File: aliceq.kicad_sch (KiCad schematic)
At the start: 174 parts, among them J1 ISP-6, SW1 SW_Push, U1 ATmega32U4-AU, U2 PRTR5V0U2X, Y1 CLK

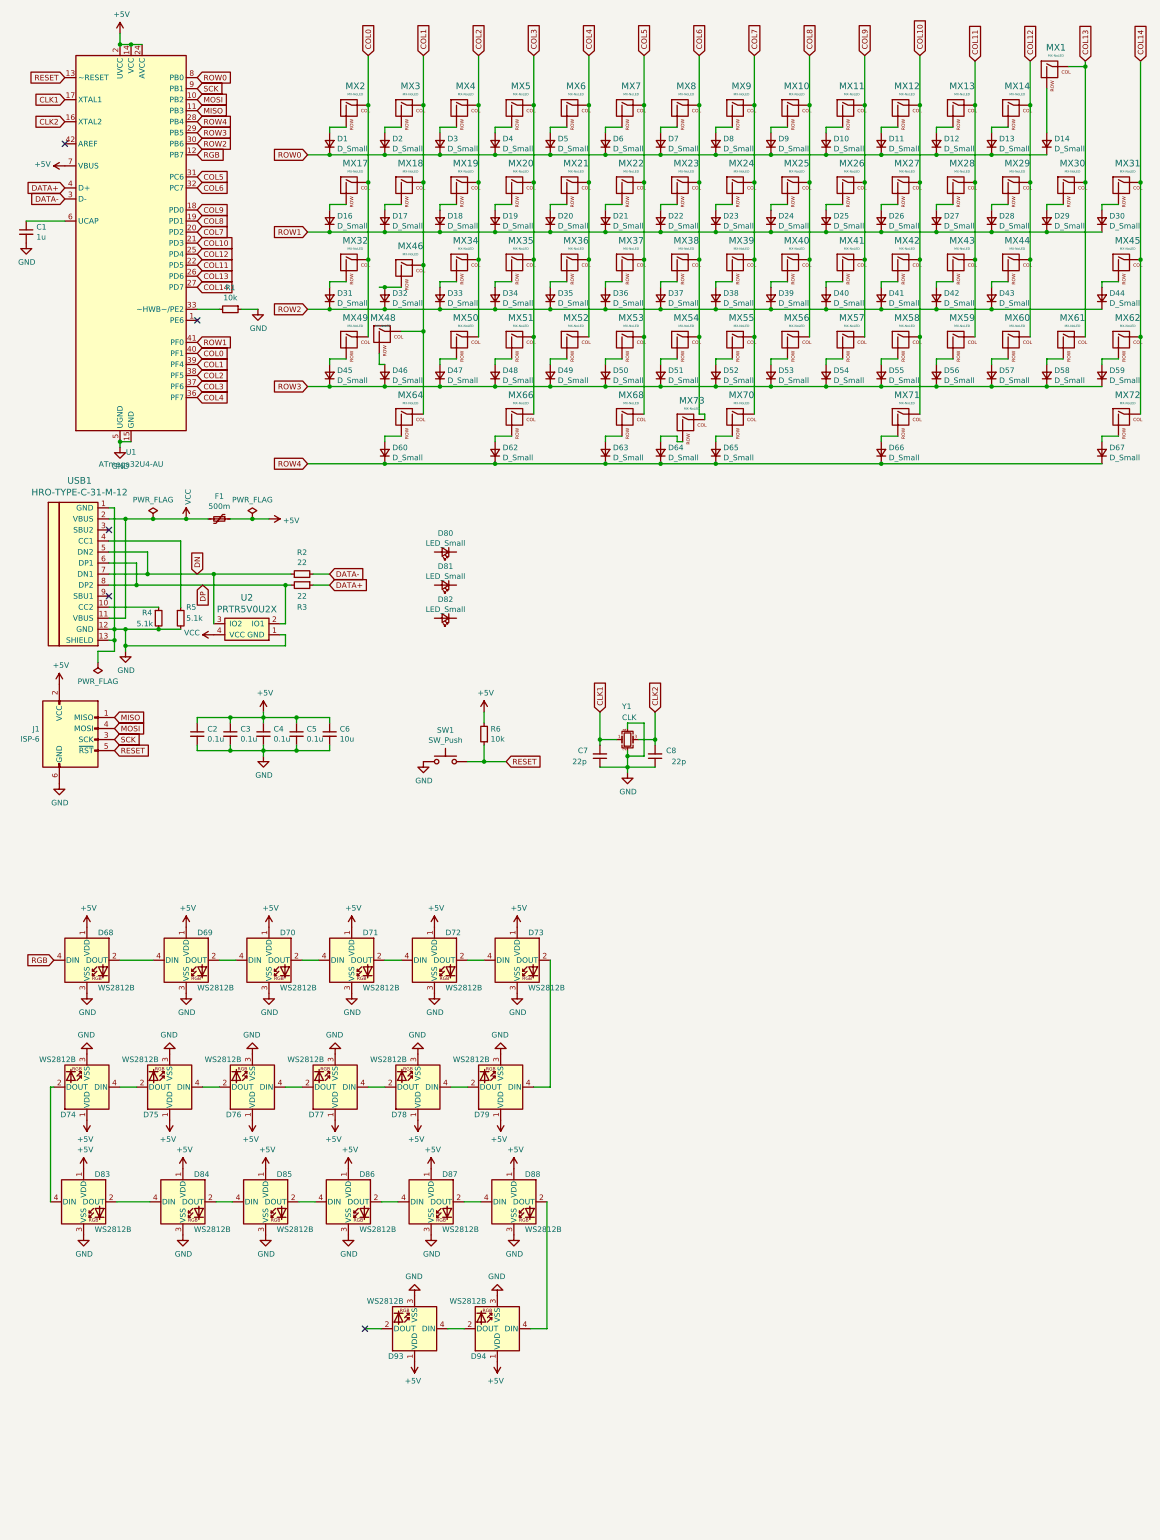
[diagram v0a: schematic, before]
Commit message: beta2
Fixed the left spacebar, added more sockets for different layout options, added rgb indicators
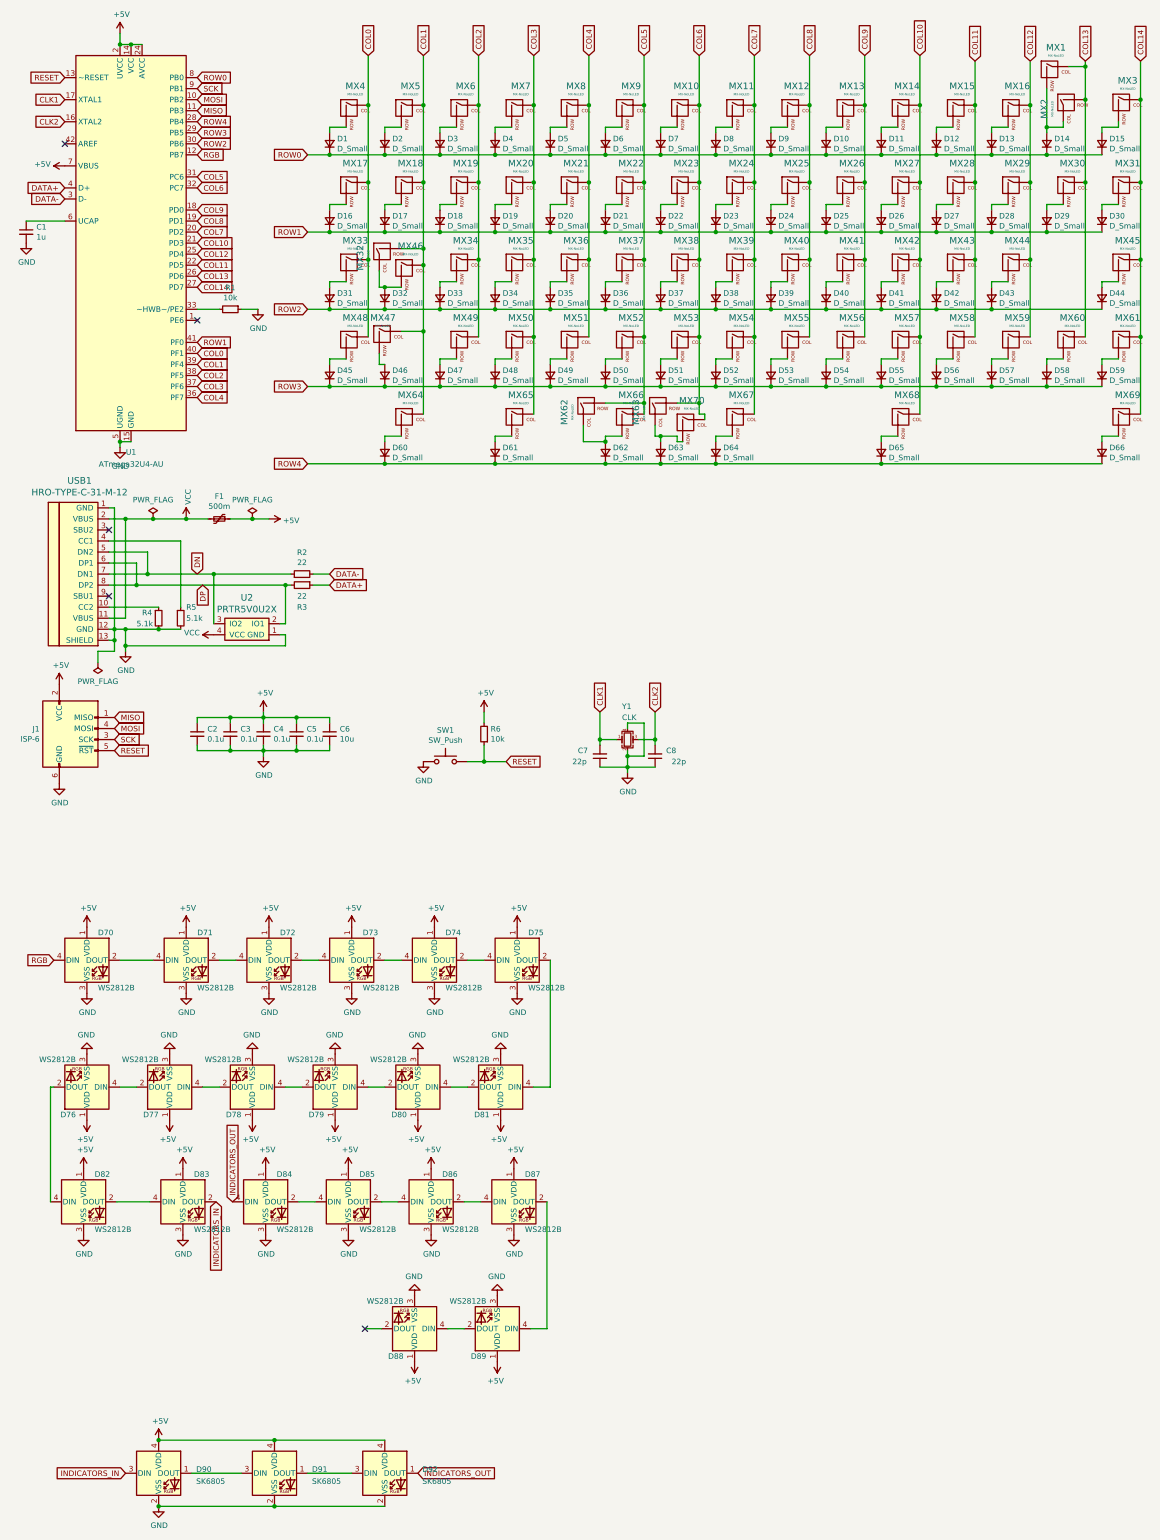
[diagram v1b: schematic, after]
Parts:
- removed D80, D81, D82: LED_Small, LED_THT:LED_D1.8mm_W3.3mm_H2.4mm, symbol Device:LED_Small
- added D15: D_Small, Diode_SMD:D_SOD-123, symbol Device:D_Small
- added D90, D91, D92: SK6805, LED_SMD:LED_SK6805_PLCC4_2.4x2.7mm_P1.3mm, symbol LED:SK6805
- added MX2, MX3, MX32, MX63: MX-NoLED, MX_Only:MXOnly-1U-Hotswap, symbol forty-rescue:MX-NoLED-MX_Alps_Hybrid
- added MX62: MX-NoLED, MX_Only:MXOnly-2.25U-Hotswap, symbol forty-rescue:MX-NoLED-MX_Alps_Hybrid
- renumbered D62 to D61, D63 to D62, D64 to D63, D65 to D64, D66 to D65, D67 to D66, D68 to D70, D69 to D71, D70 to D72, D71 to D73, D72 to D74, D73 to D75, D74 to D76, D75 to D77, D76 to D78, D77 to D79, D78 to D80, D79 to D81, D83 to D82, D84 to D83, D85 to D84, D86 to D85, D87 to D86, D88 to D87, D93 to D88, D94 to D89, MX8 to MX10, MX9 to MX11, MX10 to MX12, MX11 to MX13, MX12 to MX14, MX13 to MX15, MX14 to MX16, MX32 to MX33, MX2 to MX4, MX48 to MX47, MX49 to MX48, MX50 to MX49, MX3 to MX5, MX51 to MX50, MX52 to MX51, MX53 to MX52, MX54 to MX53, MX55 to MX54, MX56 to MX55, MX57 to MX56, MX58 to MX57, MX59 to MX58, MX60 to MX59, MX4 to MX6, MX61 to MX60, MX62 to MX61, MX66 to MX65, MX68 to MX66, MX70 to MX67, MX71 to MX68, MX72 to MX69, MX5 to MX7, MX73 to MX70, MX6 to MX8, MX7 to MX9
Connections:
- net +5V: now also D90.4 (VDD), D91.4 (VDD), D92.4 (VDD)
- net COL1: now also MX32.2 (ROW)
- net COL13: now also MX2.2 (ROW)
- net COL14: now also MX3.1 (COL)
- net COL5: now also MX62.2 (ROW)
- net COL6: now also MX63.2 (ROW)
- net GND: now also D90.2 (VSS), D91.2 (VSS), D92.2 (VSS)
- net ROW0: now also D15.1 (K)
- net at D14.2 (A), MX1.2 (ROW): now also MX2.1 (COL)
- net at D63.2 (A), MX70.2 (ROW): now also MX63.1 (COL)
- net INDICATORS_IN: now reaches D83.2 (DOUT)
- net INDICATORS_IN: now also D90.3 (DIN); no longer D84.4 (DIN)
- net at D32.2 (A), MX46.2 (ROW): now also MX32.1 (COL)
- net at D62.2 (A), MX66.2 (ROW): now also MX62.1 (COL)
- new net: D91.1 (DOUT), D92.3 (DIN)
- new net: D90.1 (DOUT), D91.3 (DIN)
- new net: D15.2 (A), MX3.2 (ROW)
- new net INDICATORS_OUT: D84.4 (DIN), D92.1 (DOUT)

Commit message: More compatibility
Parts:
- added MX71: MX-NoLED, MX_Only:MXOnly-2.75U-Hotswap-ReversedStabilizers, symbol forty-rescue:MX-NoLED-MX_Alps_Hybrid
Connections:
- net COL13: now also MX71.2 (ROW)
- net at D58.2 (A), MX60.2 (ROW): now also MX71.1 (COL)
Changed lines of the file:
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@@
   (junction (at 251.46 64.77) (diameter 1.016) (color 0 0 0 0))
   (junction (at 251.46 100.33) (diameter 1.016) (color 0 0 0 0))
+  (junction (at 255.27 93.98) (diameter 1.016) (color 0 0 0 0))
   (junction (at 260.35 26.67) (diameter 1.016) (color 0 0 0 0))
   (junction (at 260.35 34.29) (diameter 1.016) (color 0 0 0 0))
   (junction (at 260.35 53.34) (diameter 1.016) (color 0 0 0 0))
+  (junction (at 260.35 88.9) (diameter 1.016) (color 0 0 0 0))
   (junction (at 273.05 34.29) (diameter 1.016) (color 0 0 0 0))
   (junction (at 273.05 53.34) (diameter 1.016) (color 0 0 0 0))
@@
     (pin "2")
   )
+  (symbol (lib_id "forty-rescue:MX-NoLED-MX_Alps_Hybrid") (at 259.08 92.71 180) (unit 1)
+    (in_bom yes) (on_board yes)
+    (property "Reference" "MX71" (id 0) (at 258.2418 98.3742 0)
+      (effects (font (size 1.524 1.524)))
+    )
+    (property "Value" "MX-NoLED" (id 1) (at 258.2418 96.4946 0)
+      (effects (font (size 0.508 0.508)))
+    )
+    (property "Footprint" "MX_Only:MXOnly-2.75U-Hotswap-ReversedStabilizers" (id 2) (at 274.955 92.075 0)
+      (effects (font (size 1.524 1.524)) hide)
+    )
+    (property "Datasheet" "" (id 3) (at 274.955 92.075 0)
+      (effects (font (size 1.524 1.524)) hide)
+    )
+    (pin "1")
+    (pin "2")
+  )
   (symbol (lib_id "forty-rescue:MX-NoLED-MX_Alps_Hybrid") (at 269.24 35.56 0) (unit 1)
     (in_bom yes) (on_board yes)
@@
       (reference "MX70") (unit 1) (value "MX-NoLED") (footprint "MX_Only:MXOnly-1.25U-Hotswap")
     )
+    (path "/13373f14-5dcc-4b9b-80cc-eac714d4bb53"
+      (reference "MX71") (unit 1) (value "MX-NoLED") (footprint "MX_Only:MXOnly-2.75U-Hotswap-ReversedStabilizers")
+    )
     (path "/00000000-0000-0000-0000-00005fe7643d"
